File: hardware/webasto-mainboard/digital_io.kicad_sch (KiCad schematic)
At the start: 35 parts, among them Q10 DMG2301L, Q2 2N7002, Q3 2N7002, Q4 2N7002, Q5 2N7002, Q6 SUD50P04-08, Q7 SUD50P04-08, Q8 SUD50P04-08, Q9 SUD50P04-08, U4 MC33660BEFR2

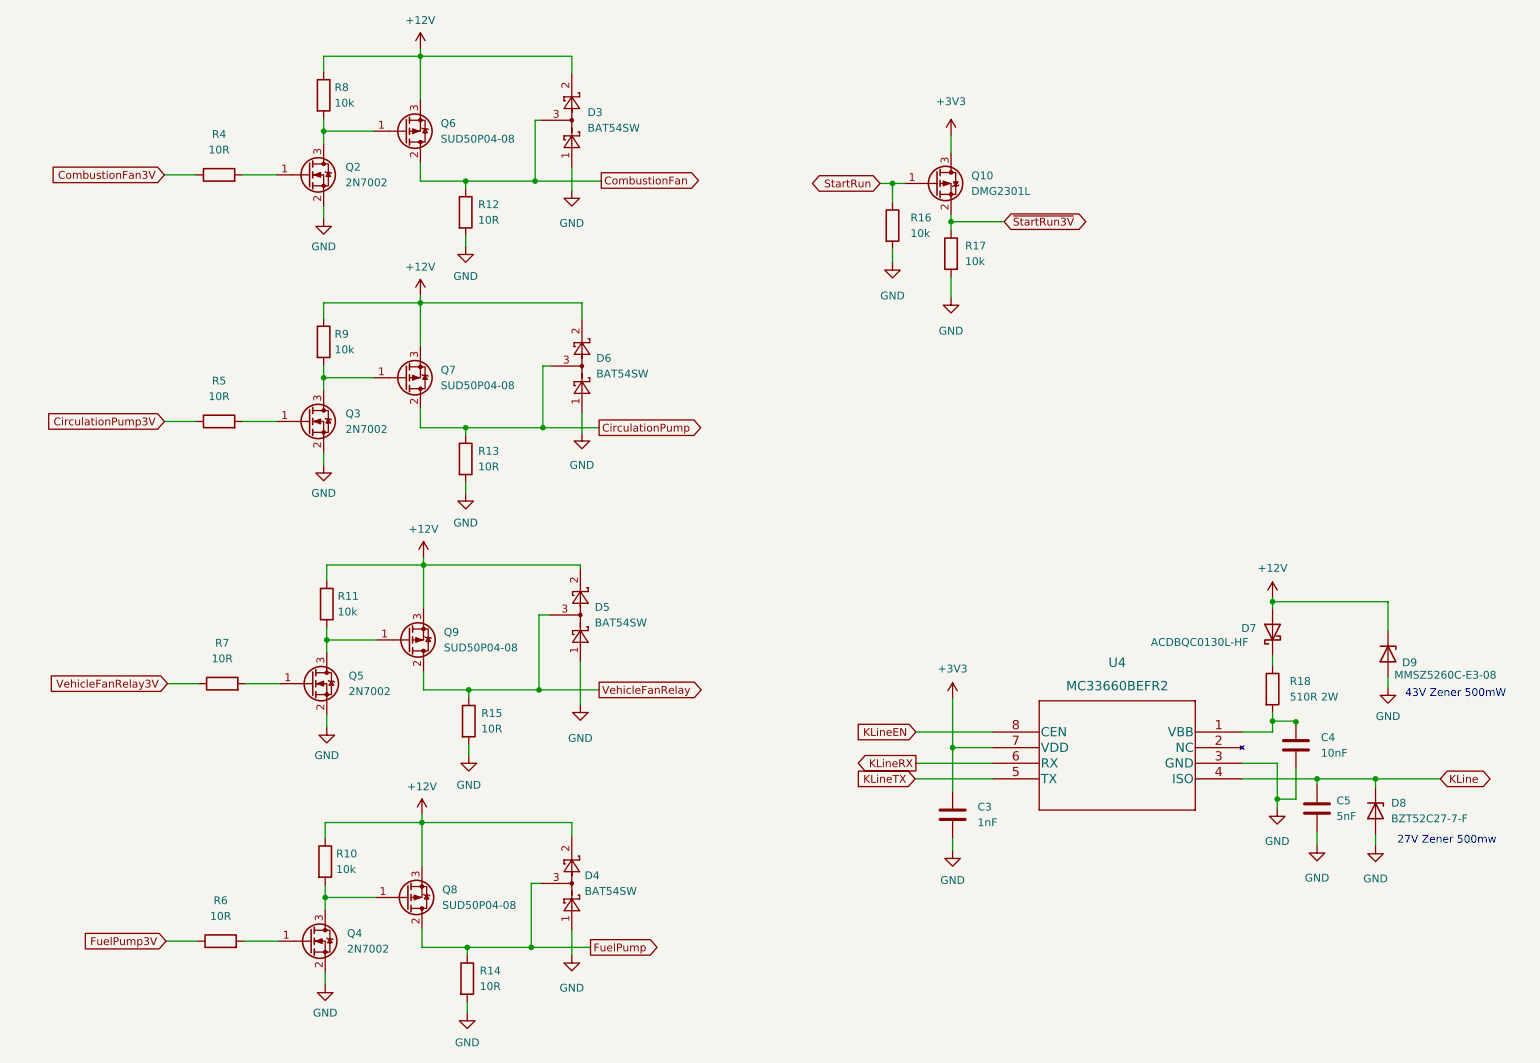
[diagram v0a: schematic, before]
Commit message: Got rid of TINY diode (0402!?!?), remove USE_USB, put in PicoW
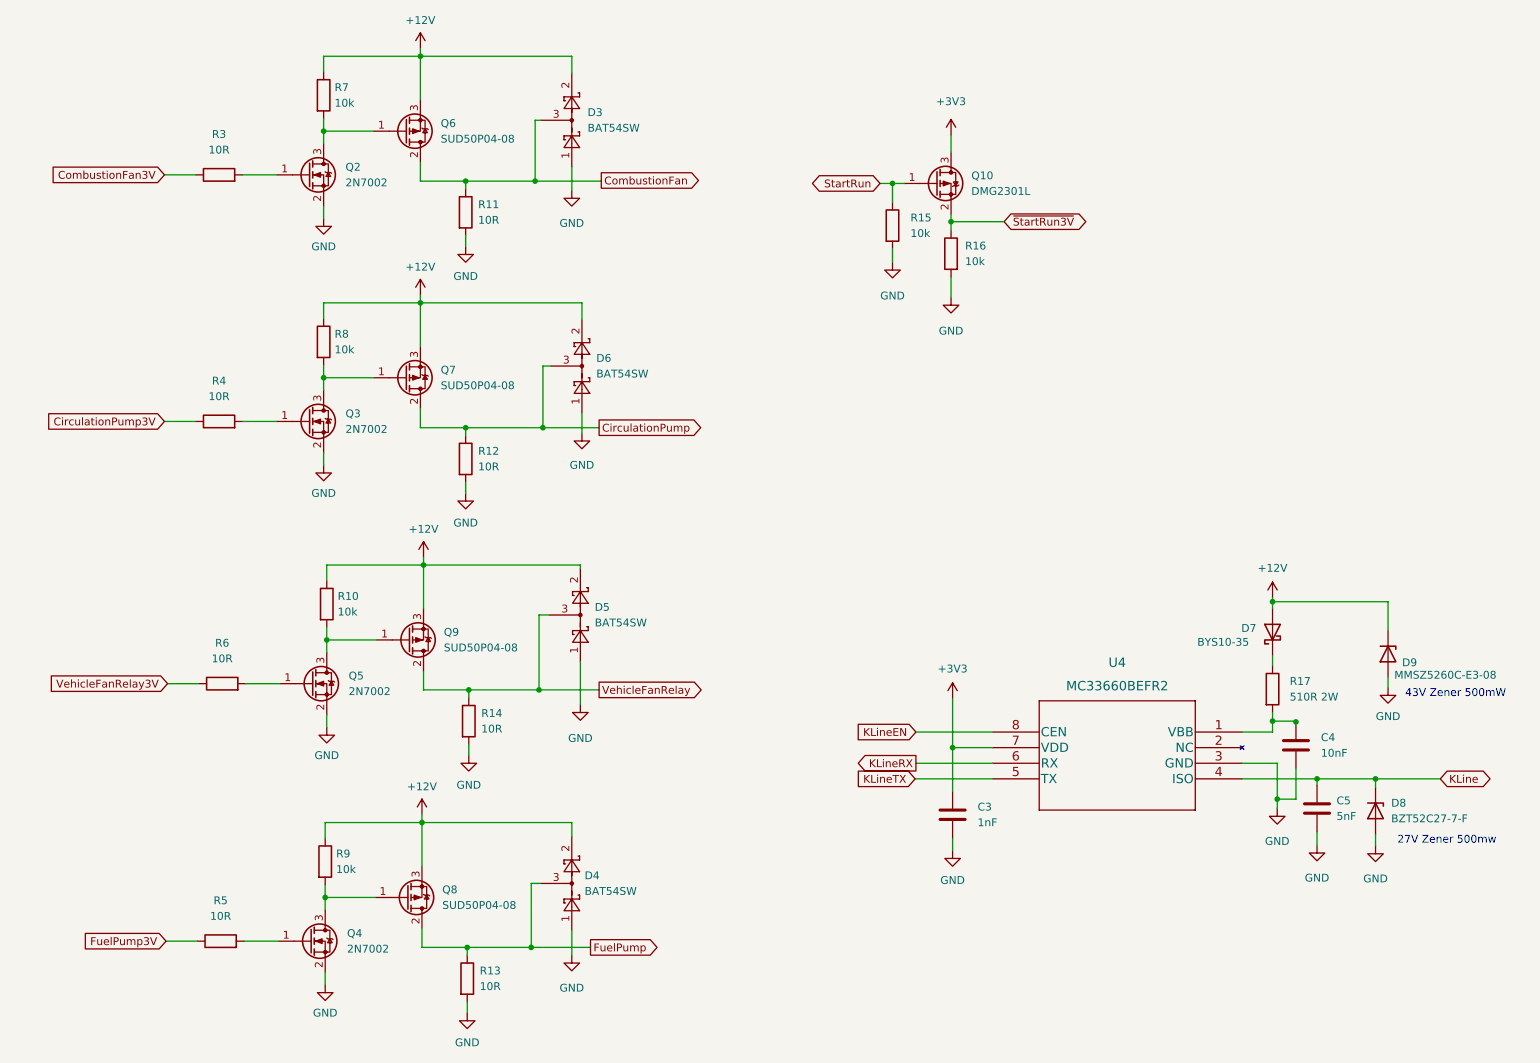
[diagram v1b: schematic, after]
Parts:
- D7: value ACDBQC0130L-HF -> BYS10-35; footprint Diode_SMD:D_SOD-923 -> Diode_SMD:D_SMA_Handsoldering
- renumbered R11 to R10, R12 to R11, R13 to R12, R14 to R13, R15 to R14, R16 to R15, R17 to R16, R18 to R17, R4 to R3, R5 to R4, R6 to R5, R7 to R6, R8 to R7, R9 to R8, R10 to R9

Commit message: Move VSYS to ADC2 to avoid the stupid WiFi setup
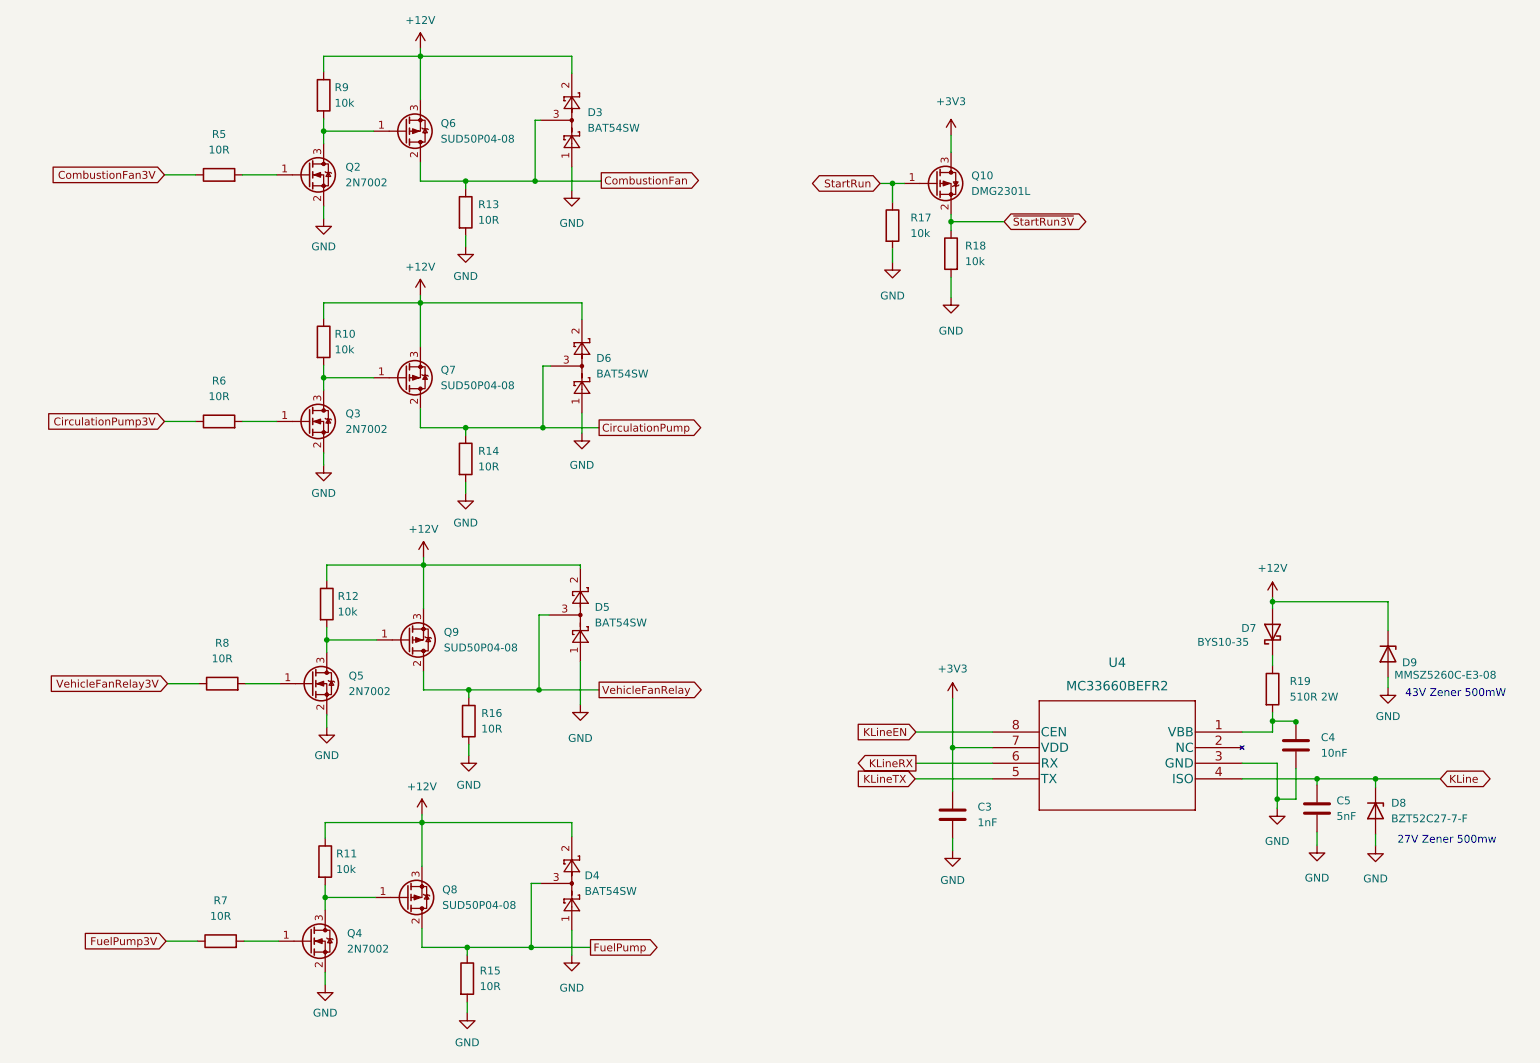
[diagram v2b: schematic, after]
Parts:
- renumbered R8 to R10, R9 to R11, R10 to R12, R11 to R13, R12 to R14, R13 to R15, R14 to R16, R15 to R17, R16 to R18, R17 to R19, R3 to R5, R4 to R6, R5 to R7, R6 to R8, R7 to R9
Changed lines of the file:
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@@
   (title_block
     (title "Webasto Replacement Mainboard (Thermo Top C)")
-    (date "2023-02-14")
+    (date "2023-02-22")
     (rev "2.0")
     (company "Gavin Hurlbut")
@@
   (symbol (lib_id "Device:R") (at 160.147 53.721 0) (unit 1)
     (in_bom yes) (on_board yes) (fields_autoplaced)
-    (property "Reference" "R15" (id 0) (at 163.068 52.4509 0)
+    (property "Reference" "R17" (id 0) (at 163.068 52.4509 0)
       (effects (font (size 1.27 1.27)) (justify left))
     )
@@
   (symbol (lib_id "Device:R") (at 50.8 170.18 90) (unit 1)
     (in_bom yes) (on_board yes) (fields_autoplaced)
-    (property "Reference" "R5" (id 0) (at 50.8 163.576 90))
+    (property "Reference" "R7" (id 0) (at 50.8 163.576 90))
     (property "Value" "10R" (id 1) (at 50.8 166.116 90))
     (property "Footprint" "Resistor_SMD:R_0805_2012Metric_Pad1.20x1.40mm_HandSolder" (id 2) (at 50.8 171.958 90)
@@
   (symbol (lib_id "Device:R") (at 67.818 157.226 0) (unit 1)
     (in_bom yes) (on_board yes) (fields_autoplaced)
-    (property "Reference" "R9" (id 0) (at 69.596 155.9559 0)
+    (property "Reference" "R11" (id 0) (at 69.596 155.9559 0)
       (effects (font (size 1.27 1.27)) (justify left))
     )
@@
   (symbol (lib_id "Device:R") (at 90.932 176.276 0) (unit 1)
     (in_bom yes) (on_board yes) (fields_autoplaced)
-    (property "Reference" "R13" (id 0) (at 92.964 175.0059 0)
+    (property "Reference" "R15" (id 0) (at 92.964 175.0059 0)
       (effects (font (size 1.27 1.27)) (justify left))
     )
@@
   (symbol (lib_id "Device:R") (at 91.186 134.366 0) (unit 1)
     (in_bom yes) (on_board yes) (fields_autoplaced)
-    (property "Reference" "R14" (id 0) (at 93.218 133.0959 0)
+    (property "Reference" "R16" (id 0) (at 93.218 133.0959 0)
       (effects (font (size 1.27 1.27)) (justify left))
     )
@@
   (symbol (lib_id "Device:R") (at 50.546 45.466 90) (unit 1)
     (in_bom yes) (on_board yes) (fields_autoplaced)
-    (property "Reference" "R3" (id 0) (at 50.546 38.862 90))
+    (property "Reference" "R5" (id 0) (at 50.546 38.862 90))
     (property "Value" "10R" (id 1) (at 50.546 41.402 90))
     (property "Footprint" "Resistor_SMD:R_0805_2012Metric_Pad1.20x1.40mm_HandSolder" (id 2) (at 50.546 47.244 90)
@@
   (symbol (lib_id "Device:R") (at 68.072 115.316 0) (unit 1)
     (in_bom yes) (on_board yes) (fields_autoplaced)
-    (property "Reference" "R10" (id 0) (at 69.85 114.0459 0)
+    (property "Reference" "R12" (id 0) (at 69.85 114.0459 0)
       (effects (font (size 1.27 1.27)) (justify left))
     )
@@
   (symbol (lib_id "Device:R") (at 90.678 91.694 0) (unit 1)
     (in_bom yes) (on_board yes) (fields_autoplaced)
-    (property "Reference" "R12" (id 0) (at 92.71 90.4239 0)
+    (property "Reference" "R14" (id 0) (at 92.71 90.4239 0)
       (effects (font (size 1.27 1.27)) (justify left))
     )
@@
   (symbol (lib_id "Device:R") (at 50.546 85.598 90) (unit 1)
     (in_bom yes) (on_board yes) (fields_autoplaced)
-    (property "Reference" "R4" (id 0) (at 50.546 78.994 90))
+    (property "Reference" "R6" (id 0) (at 50.546 78.994 90))
     (property "Value" "10R" (id 1) (at 50.546 81.534 90))
     (property "Footprint" "Resistor_SMD:R_0805_2012Metric_Pad1.20x1.40mm_HandSolder" (id 2) (at 50.546 87.376 90)
@@
   (symbol (lib_id "Device:R") (at 169.672 58.293 0) (mirror y) (unit 1)
     (in_bom yes) (on_board yes) (fields_autoplaced)
-    (property "Reference" "R16" (id 0) (at 171.958 57.0229 0)
+    (property "Reference" "R18" (id 0) (at 171.958 57.0229 0)
       (effects (font (size 1.27 1.27)) (justify right))
     )
@@
   (symbol (lib_id "Device:R") (at 67.564 72.644 0) (unit 1)
     (in_bom yes) (on_board yes) (fields_autoplaced)
-    (property "Reference" "R8" (id 0) (at 69.342 71.3739 0)
+    (property "Reference" "R10" (id 0) (at 69.342 71.3739 0)
       (effects (font (size 1.27 1.27)) (justify left))
     )
@@
   (symbol (lib_id "Device:R") (at 90.678 51.562 0) (unit 1)
     (in_bom yes) (on_board yes) (fields_autoplaced)
-    (property "Reference" "R11" (id 0) (at 92.71 50.2919 0)
+    (property "Reference" "R13" (id 0) (at 92.71 50.2919 0)
       (effects (font (size 1.27 1.27)) (justify left))
     )
@@
   (symbol (lib_id "Device:R") (at 51.054 128.27 90) (unit 1)
     (in_bom yes) (on_board yes) (fields_autoplaced)
-    (property "Reference" "R6" (id 0) (at 51.054 121.666 90))
+    (property "Reference" "R8" (id 0) (at 51.054 121.666 90))
     (property "Value" "10R" (id 1) (at 51.054 124.206 90))
     (property "Footprint" "Resistor_SMD:R_0805_2012Metric_Pad1.20x1.40mm_HandSolder" (id 2) (at 51.054 130.048 90)
@@
   (symbol (lib_id "Device:R") (at 67.564 32.512 0) (unit 1)
     (in_bom yes) (on_board yes) (fields_autoplaced)
-    (property "Reference" "R7" (id 0) (at 69.342 31.2419 0)
+    (property "Reference" "R9" (id 0) (at 69.342 31.2419 0)
       (effects (font (size 1.27 1.27)) (justify left))
     )
@@
   (symbol (lib_id "Device:R") (at 221.996 129.159 0) (unit 1)
     (in_bom yes) (on_board yes) (fields_autoplaced)
-    (property "Reference" "R17" (id 0) (at 224.79 127.8889 0)
-      (effects (font (size 1.27 1.27)) (justify left))
-    )
+    (property "Reference" "R19" (id 0) (at 224.79 127.8889 0)
+      (effects (font (size 1.27 1.27)) (justify left))
+    )

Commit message: Move the LED to the mainboard
- due to how the driver doesn't share the SPI bus well, you currently can
  either use the TCP stack or the GPIOs.  Mixing will cause weird crashes.
- so I'm adding the LED onto the mainboard directly.
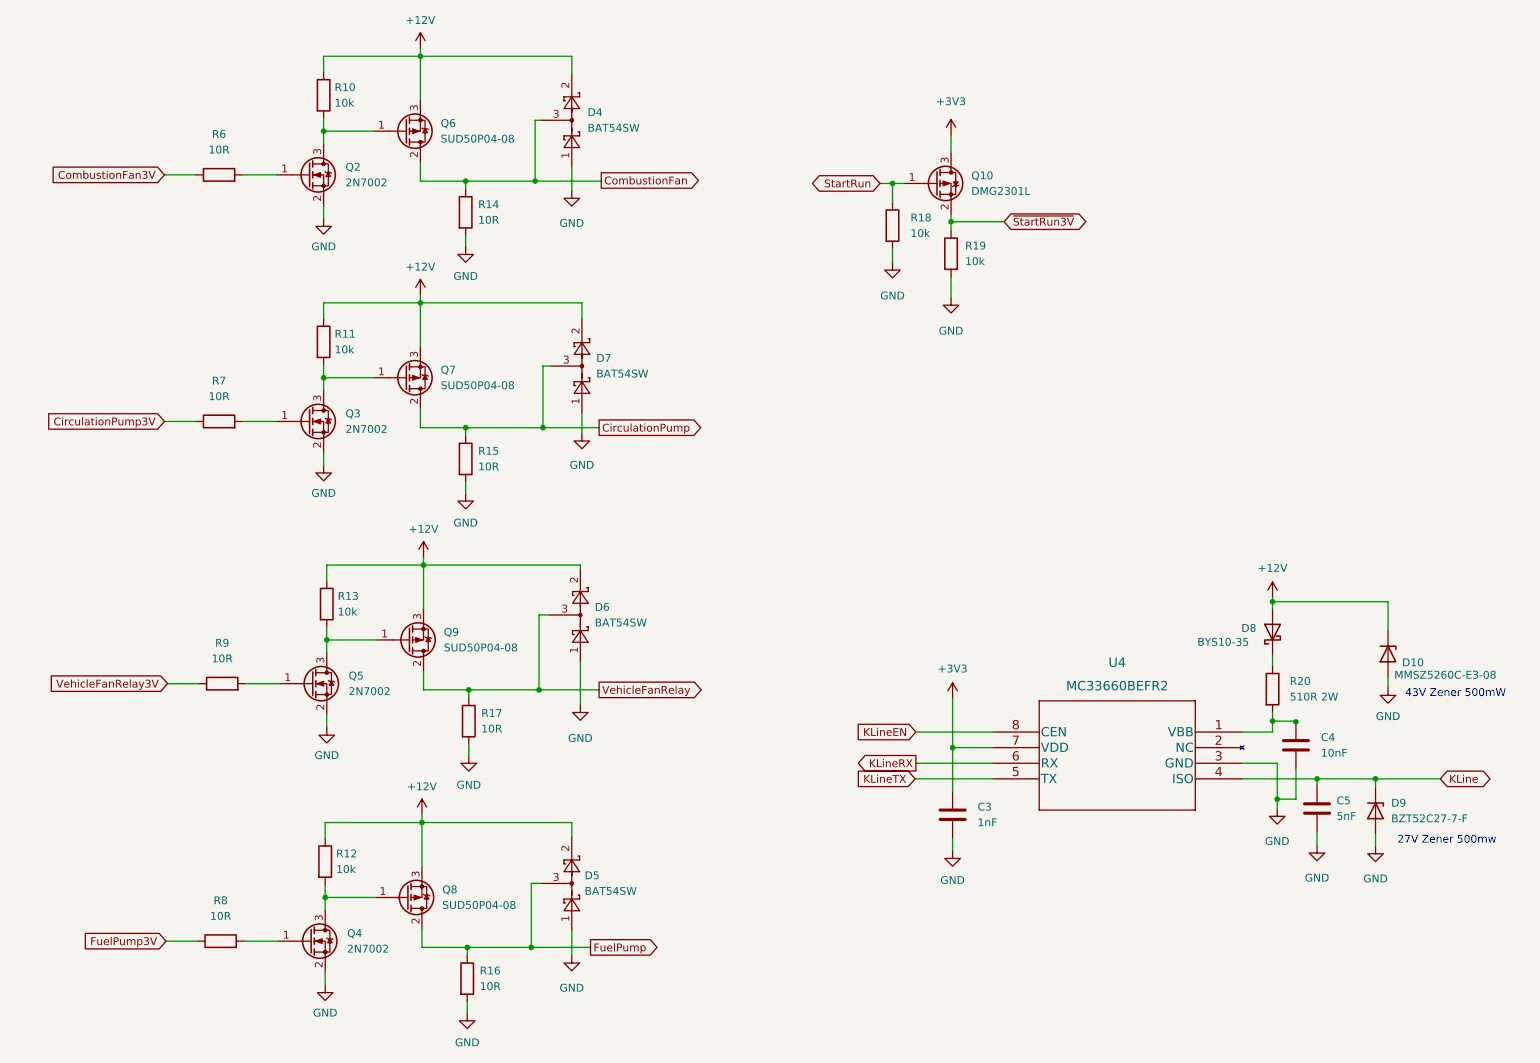
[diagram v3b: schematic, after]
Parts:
- renumbered D9 to D10, D3 to D4, D4 to D5, D5 to D6, D6 to D7, D7 to D8, D8 to D9, R9 to R10, R10 to R11, R11 to R12, R12 to R13, R13 to R14, R14 to R15, R15 to R16, R16 to R17, R17 to R18, R18 to R19, R19 to R20, R5 to R6, R6 to R7, R7 to R8, R8 to R9
